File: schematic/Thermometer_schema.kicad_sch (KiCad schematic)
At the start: 13 parts, among them J1 USB C, SW1 SW_Push, U1 ESP-12F, U2 SHT21, U3 SSD1306

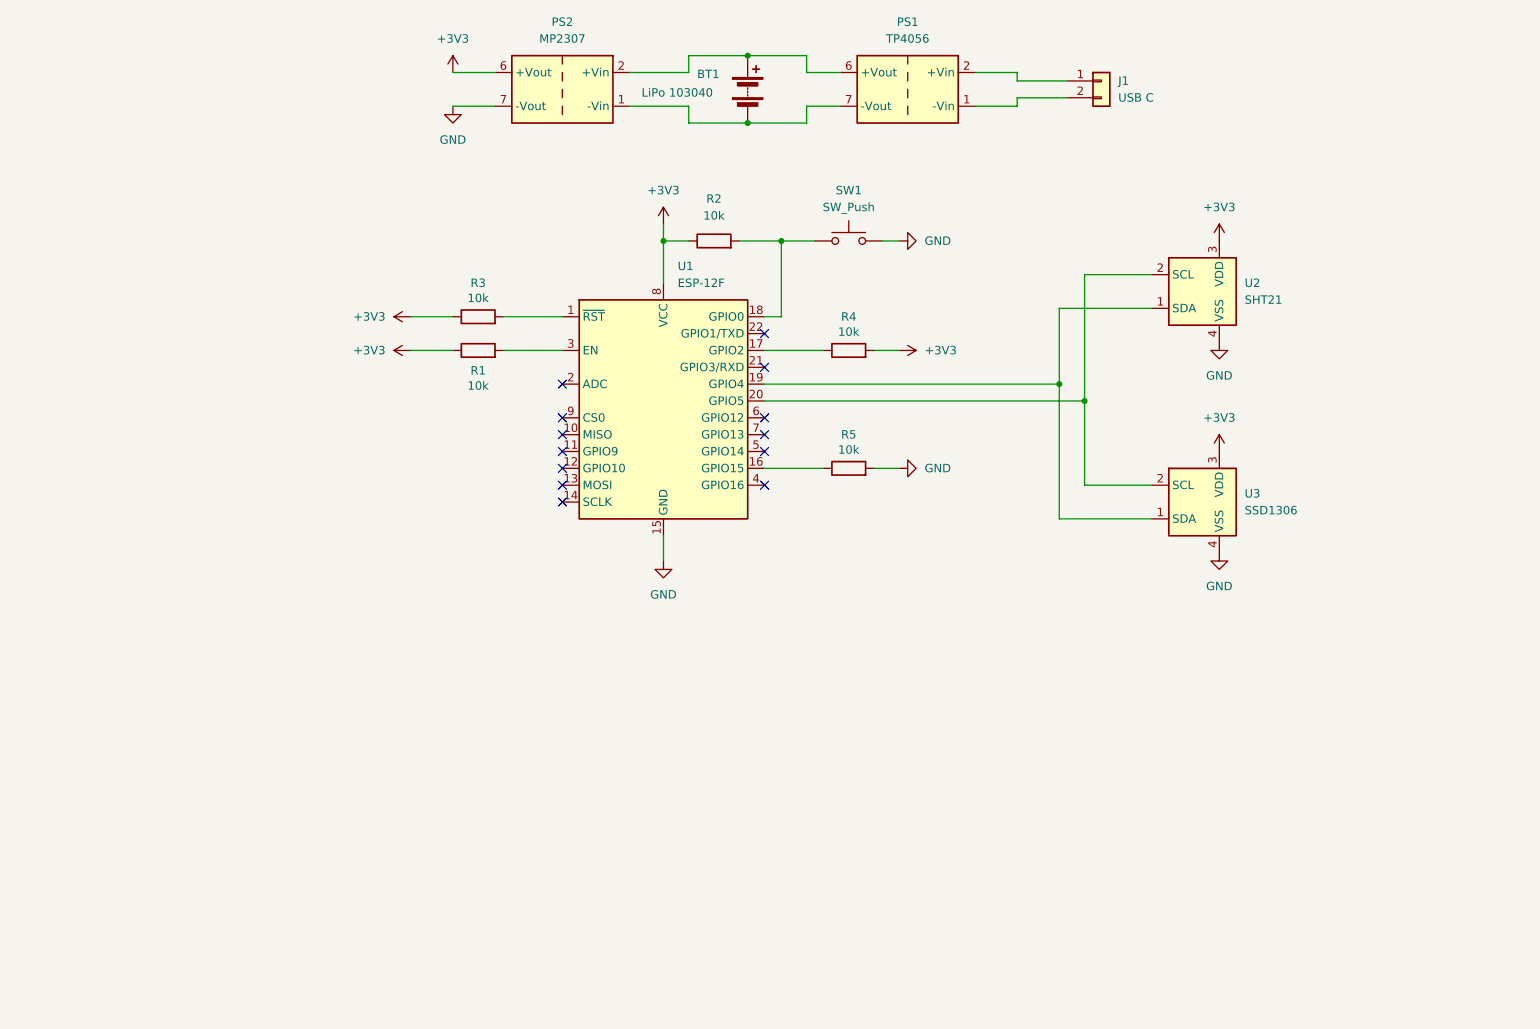
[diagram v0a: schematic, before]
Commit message: Schematic rework + reorganizing workspace
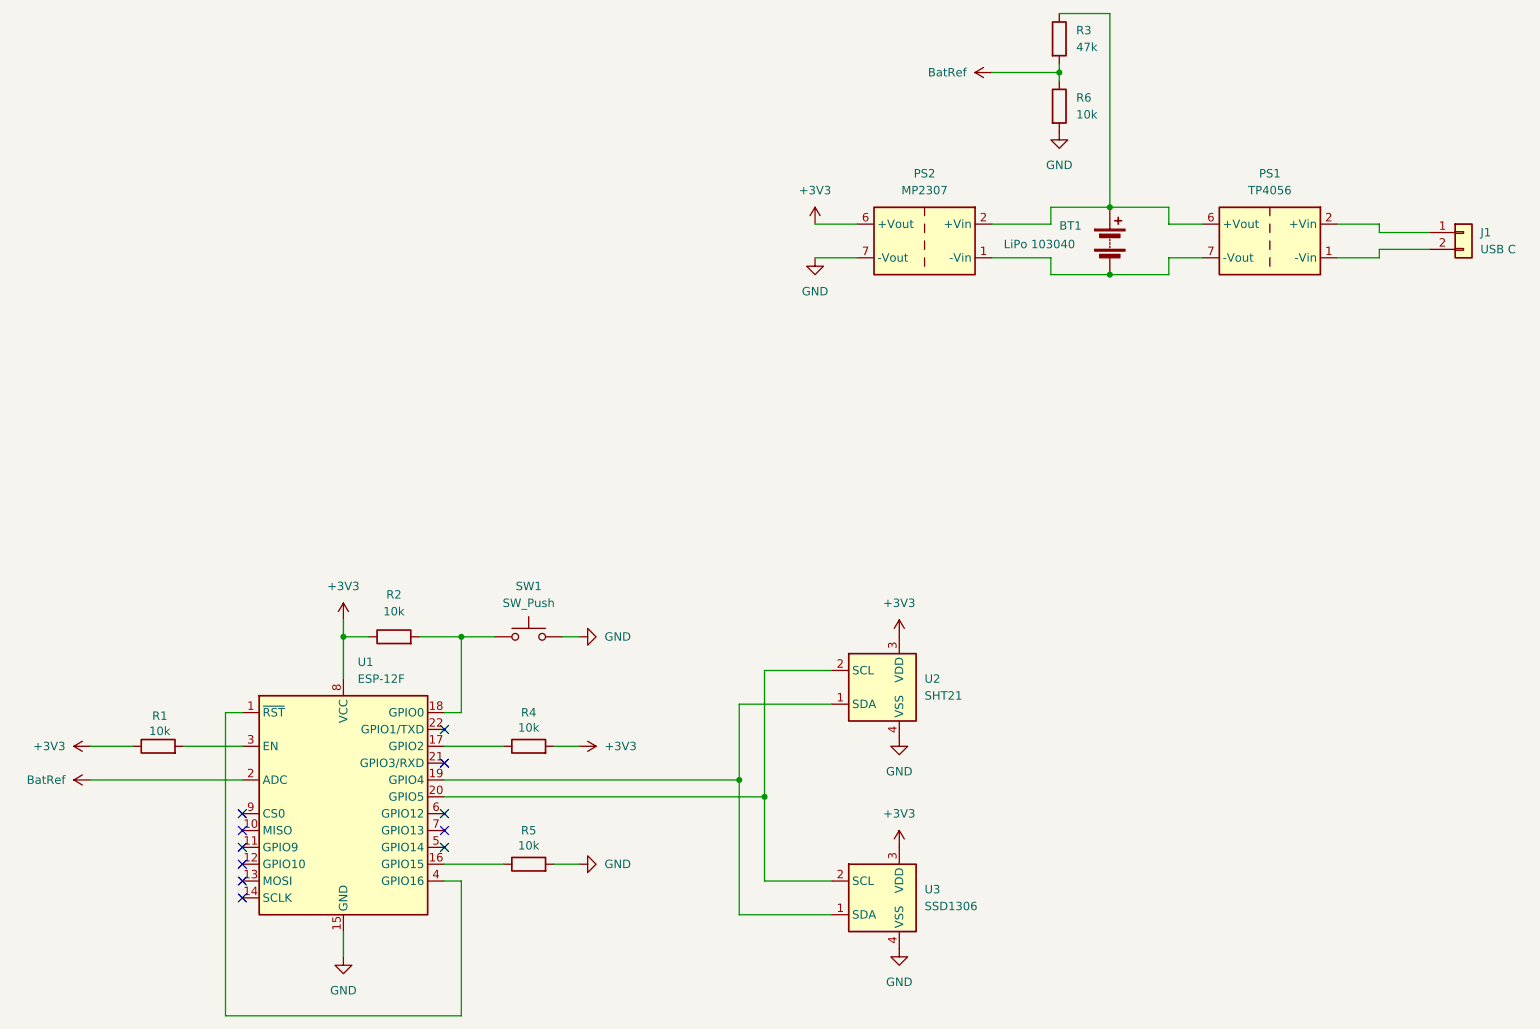
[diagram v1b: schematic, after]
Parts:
- added R6: 10k, symbol Device:R
- R3: value 10k -> 47k
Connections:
- net +3V3: no longer R3.1
- net GND: now also R6.2
- net at U1.1 (~{RST}): now also U1.4 (GPIO16); no longer R3.2
- net at BT1.1 (+), PS1.6 (+Vout), PS2.2 (+Vin): now also R3.1
- net BatRef: now reaches U1.2 (ADC)
- net BatRef: now also R3.2, R6.1
- no-connect marks 13 -> 11
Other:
- moved on the sheet: BT1, J1, PS1, PS2, R1, R2, R4, R5, SW1, U1, U2, U3

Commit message: Sleep mode (faulty)
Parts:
- removed R2: 10k, symbol Device:R
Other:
- moved on the sheet: BT1, J1, PS1, PS2, R1, R3, R4, R5, R6, SW1, U1, U2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

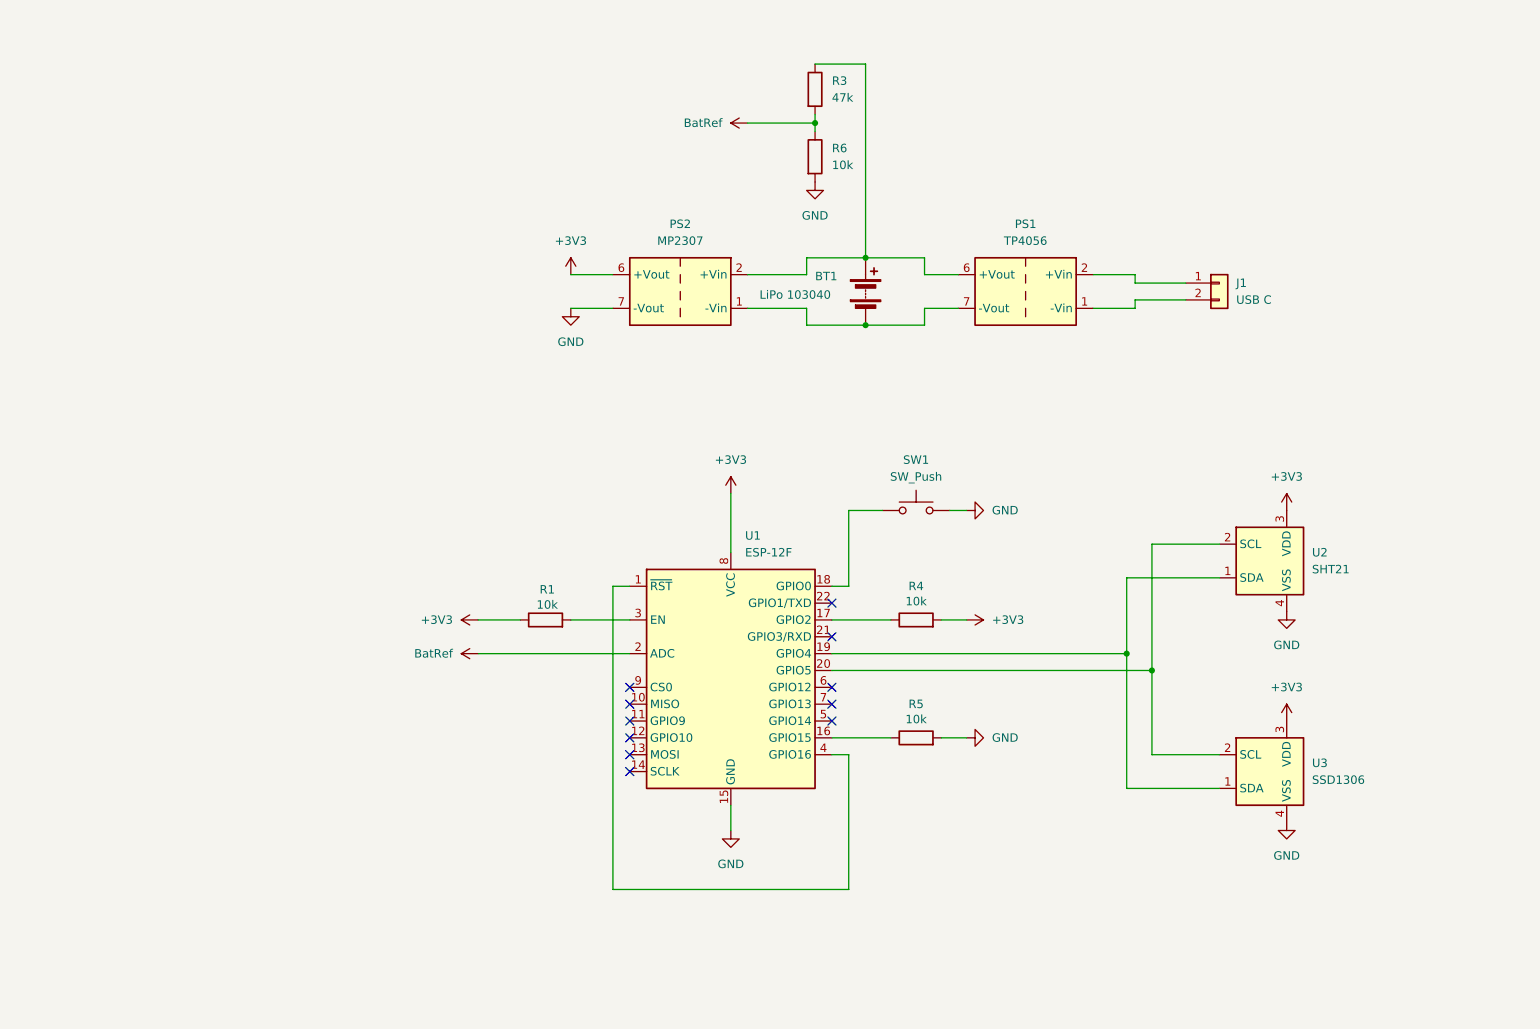
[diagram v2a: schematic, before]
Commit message: Schematic changes
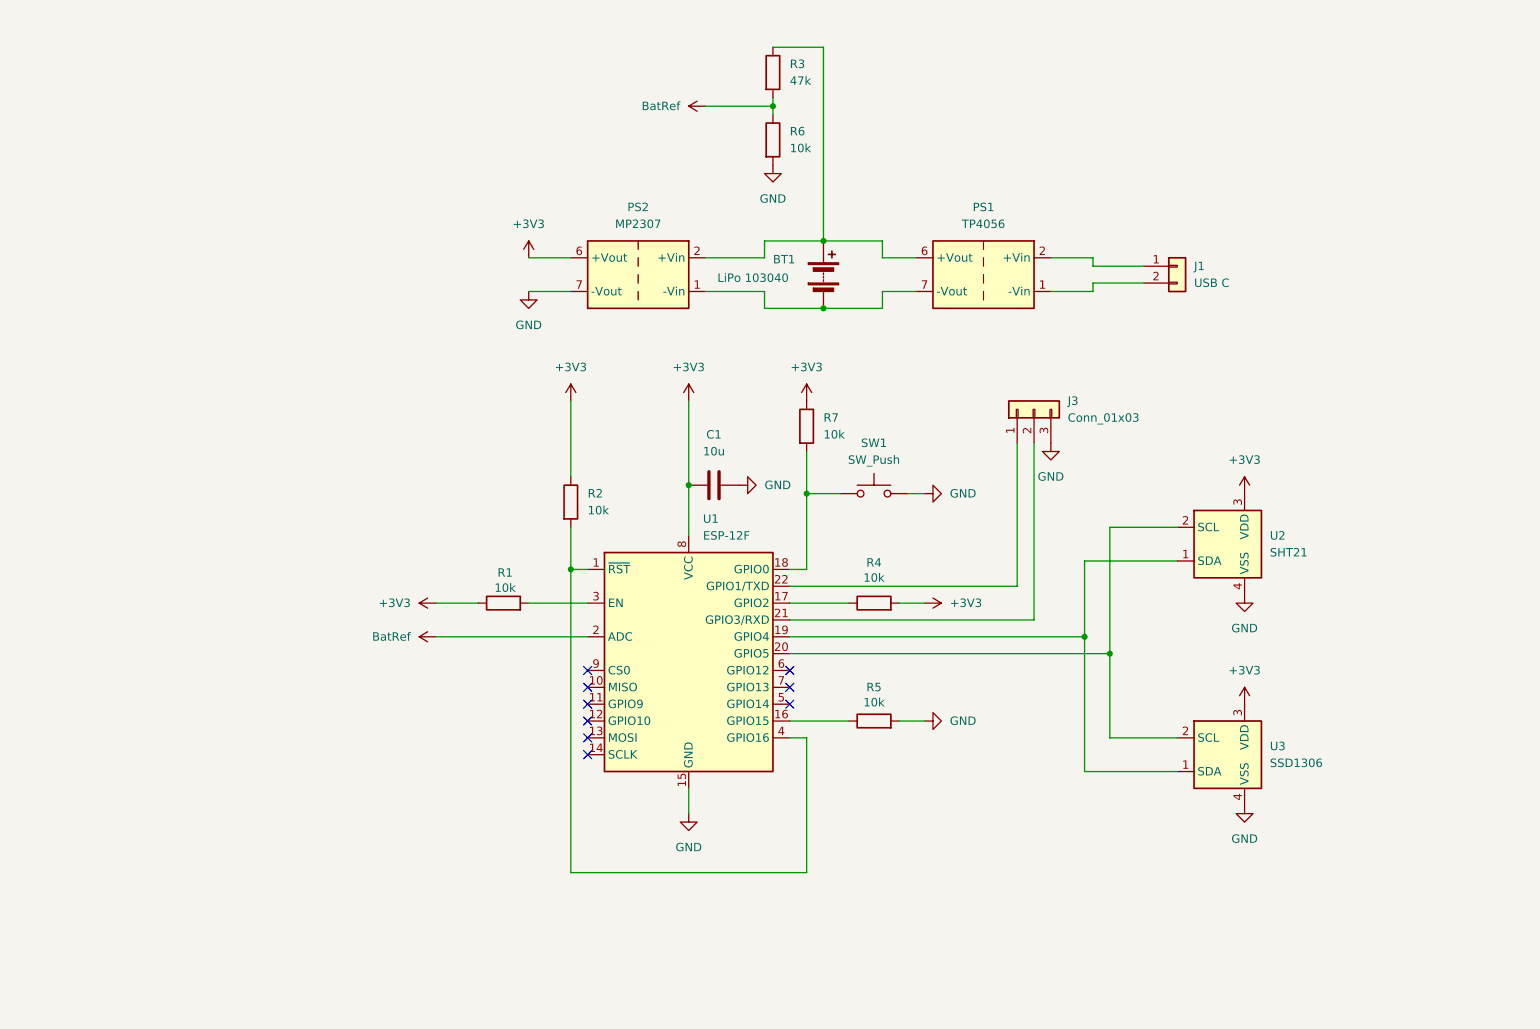
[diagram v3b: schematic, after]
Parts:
- added C1: 10u, symbol Device:C
- added J3: Conn_01x03, symbol Connector_Generic:Conn_01x03
- added R2, R7: 10k, symbol Device:R
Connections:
- net +3V3: now also C1.1, R2.1, R7.1
- net GND: now also C1.2, J3.3 (Pin_3)
- net at SW1.1, U1.18 (GPIO0): now also R7.2
- net at U1.1 (~{RST}), U1.4 (GPIO16): now also R2.2
- net at U1.21 (GPIO3/RXD): now also J3.2 (Pin_2)
- net at U1.22 (GPIO1/TXD): now also J3.1 (Pin_1)
- no-connect marks 11 -> 9
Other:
- moved on the sheet: BT1, J1, PS1, PS2, R1, R3, R4, R5, R6, SW1, U1, U2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

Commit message: Schematic update
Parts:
- added SW2, SW3: SW_Push, symbol Switch:SW_Push
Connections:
- net GND: now also SW2.1, SW3.1
- net at R2.2, U1.1 (~{RST}): now also SW2.2; no longer U1.4 (GPIO16)
- new net: SW3.2, U1.4 (GPIO16)
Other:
- moved on the sheet: PS1
